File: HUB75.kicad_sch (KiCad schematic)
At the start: 12 parts, among them J2 Conn_02x08_Odd_Even, U10 SN74LVC8T245, U11 SN74LVC8T245, U2 ICE40HX8K-BG121

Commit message: Routing changes, pullups, etc
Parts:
- C30, C37, C38, J2, JP2, U10, U11, U2: Source (none) -> ANY
- R16, R17, R18, R19: value R -> 10k; Source (none) -> ANY
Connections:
- net GND: now also R16.1, R17.1
- net VCC: no longer R16.1, R17.1

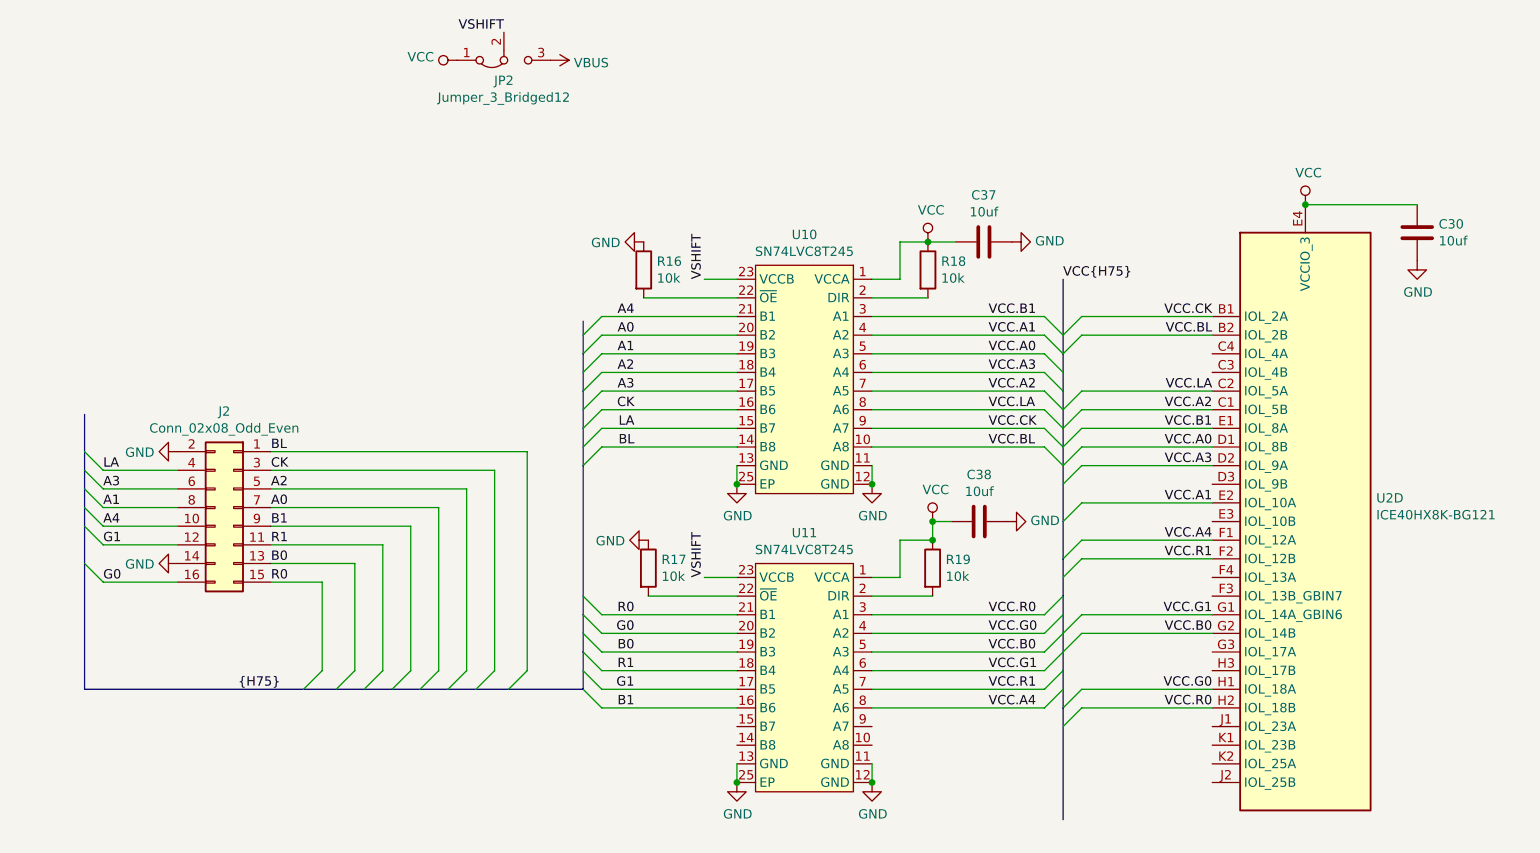
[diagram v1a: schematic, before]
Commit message: Routing cleanup, fix primary transformer
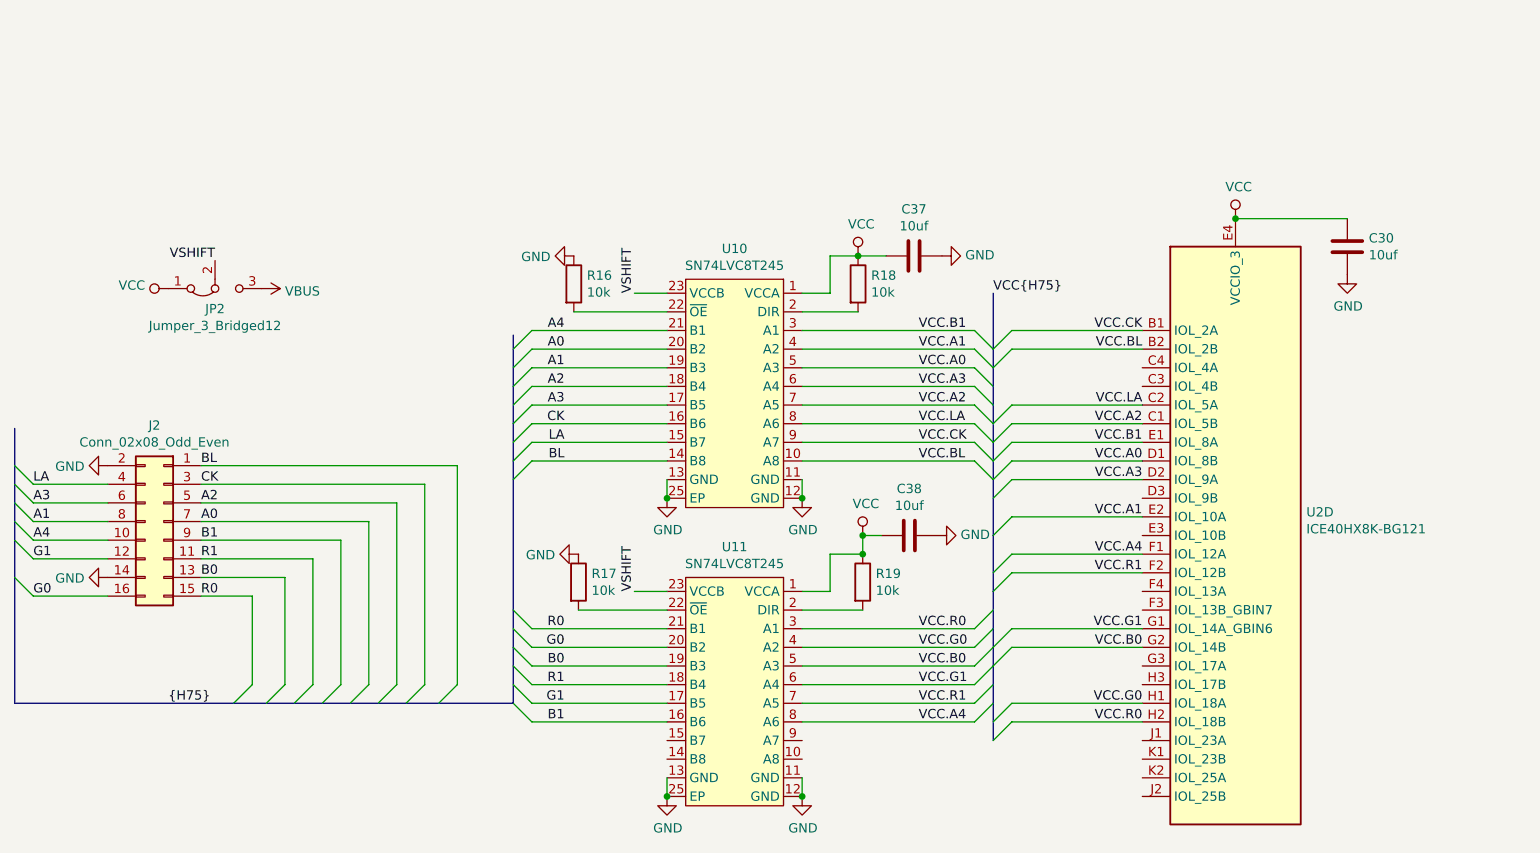
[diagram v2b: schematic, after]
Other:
- moved on the sheet: C30, C37, C38, J2, JP2, R16, R17, R18, R19, U10, U11, U2D

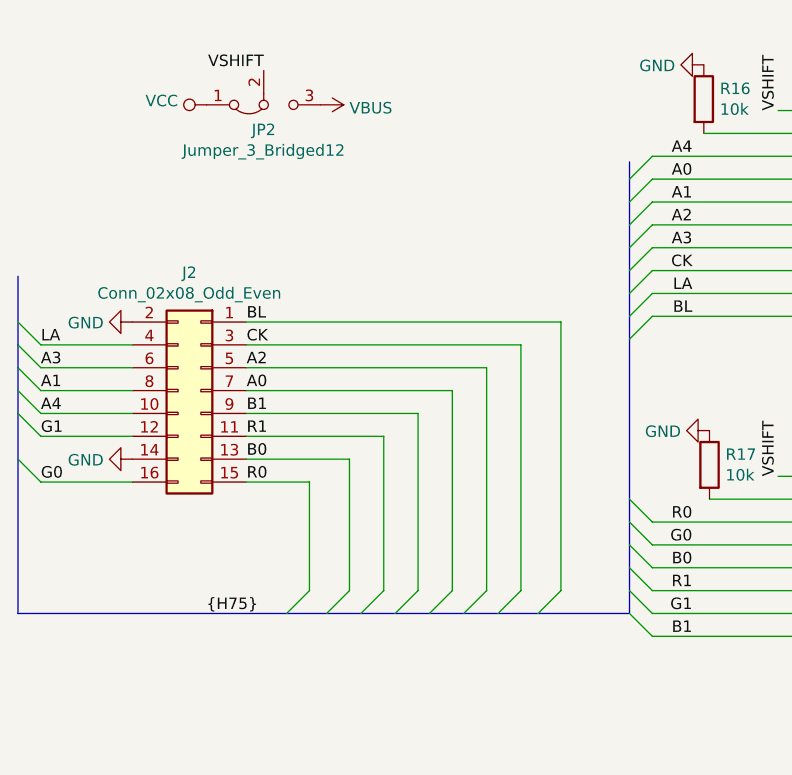
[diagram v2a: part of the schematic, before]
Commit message: Change PoE controller to NCP1081
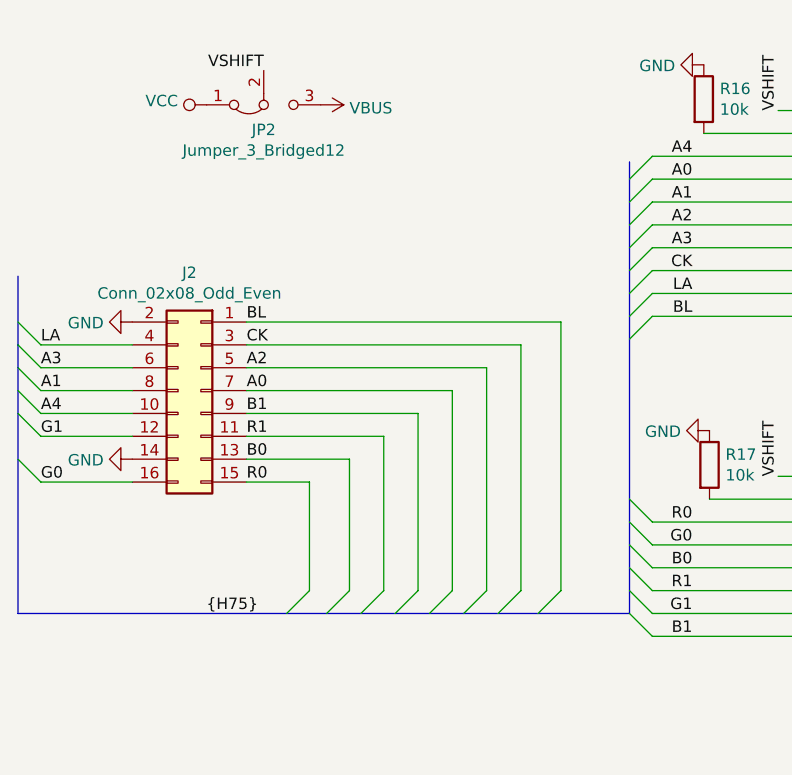
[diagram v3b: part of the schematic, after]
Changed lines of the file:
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@@
-(kicad_sch (version 20200512) (host eeschema "5.99.0-unknown-eae0c14~101~ubuntu20.04.1")
-  (page 7 7)
+(kicad_sch (version 20200608) (host eeschema "5.99.0-unknown-8bd9b26~101~ubuntu20.04.1")
+  (page 1 7)
   (paper "A4")
   (title_block
@@
     (stroke (width 0) (type solid) (color 0 0 0 0))
   )
-  (bus (pts (xy 53.34 129.54) (xy 83.185 129.54))
-    (stroke (width 0) (type solid) (color 0 0 0 0))
-  )
-  (bus (pts (xy 83.185 129.54) (xy 91.44 129.54))
-    (stroke (width 0) (type solid) (color 0 0 0 0))
-  )
-  (bus (pts (xy 91.44 129.54) (xy 99.06 129.54))
-    (stroke (width 0) (type solid) (color 0 0 0 0))
-  )
-  (bus (pts (xy 99.06 129.54) (xy 106.68 129.54))
-    (stroke (width 0) (type solid) (color 0 0 0 0))
-  )
-  (bus (pts (xy 106.68 129.54) (xy 121.285 129.54))
-    (stroke (width 0) (type solid) (color 0 0 0 0))
-  )
-  (bus (pts (xy 121.285 79.375) (xy 121.285 81.28))
-    (stroke (width 0) (type solid) (color 0 0 0 0))
-  )
-  (bus (pts (xy 121.285 81.28) (xy 121.285 86.36))
-    (stroke (width 0) (type solid) (color 0 0 0 0))
-  )
-  (bus (pts (xy 121.285 86.36) (xy 121.285 91.44))
+  (bus (pts (xy 53.34 129.54) (xy 87.63 129.54))
+    (stroke (width 0) (type solid) (color 0 0 0 0))
+  )
+  (bus (pts (xy 87.63 129.54) (xy 95.25 129.54))
+    (stroke (width 0) (type solid) (color 0 0 0 0))
+  )
+  (bus (pts (xy 95.25 129.54) (xy 102.87 129.54))
+    (stroke (width 0) (type solid) (color 0 0 0 0))
+  )
+  (bus (pts (xy 102.87 129.54) (xy 111.125 129.54))
+    (stroke (width 0) (type solid) (color 0 0 0 0))
+  )
+  (bus (pts (xy 111.125 129.54) (xy 121.285 129.54))
+    (stroke (width 0) (type solid) (color 0 0 0 0))
+  )
+  (bus (pts (xy 121.285 79.375) (xy 121.285 83.82))
+    (stroke (width 0) (type solid) (color 0 0 0 0))
+  )
+  (bus (pts (xy 121.285 83.82) (xy 121.285 88.9))
+    (stroke (width 0) (type solid) (color 0 0 0 0))
+  )
+  (bus (pts (xy 121.285 88.9) (xy 121.285 91.44))
     (stroke (width 0) (type solid) (color 0 0 0 0))
   )
@@
     (stroke (width 0) (type solid) (color 0 0 0 0))
   )
-  (bus (pts (xy 121.285 121.92) (xy 121.285 124.46))
-    (stroke (width 0) (type solid) (color 0 0 0 0))
-  )
-  (bus (pts (xy 121.285 124.46) (xy 121.285 129.54))
+  (bus (pts (xy 121.285 121.92) (xy 121.285 127))
+    (stroke (width 0) (type solid) (color 0 0 0 0))
+  )
+  (bus (pts (xy 121.285 127) (xy 121.285 129.54))
     (stroke (width 0) (type solid) (color 0 0 0 0))
   )
@@
   )
   (symbol (lib_id "power:VCC") (at 74.295 73.025 90) (unit 1)
+    (in_bom yes) (on_board yes)
     (property "Reference" "#PWR0160" (id 0) (at 78.105 73.025 0)
       (effects (font (size 1.27 1.27)) hide)
@@
   )
   (symbol (lib_id "power:VCC") (at 168.275 68.58 0) (unit 1)
+    (in_bom yes) (on_board yes)
     (property "Reference" "#PWR0158" (id 0) (at 168.275 72.39 0)
       (effects (font (size 1.27 1.27)) hide)
@@
   )
   (symbol (lib_id "power:VCC") (at 168.91 106.68 0) (unit 1)
+    (in_bom yes) (on_board yes)
     (property "Reference" "#PWR0157" (id 0) (at 168.91 110.49 0)
       (effects (font (size 1.27 1.27)) hide)
@@
   )
   (symbol (lib_id "power:VCC") (at 219.71 63.5 0) (unit 1)
+    (in_bom yes) (on_board yes)
     (property "Reference" "#PWR0137" (id 0) (at 219.71 67.31 0)
       (effects (font (size 1.27 1.27)) hide)
@@
   )
   (symbol (lib_id "power:VBUS") (at 86.995 73.025 270) (unit 1)
+    (in_bom yes) (on_board yes)
     (property "Reference" "#PWR0156" (id 0) (at 83.185 73.025 0)
       (effects (font (size 1.27 1.27)) hide)
@@
   )
   (symbol (lib_id "power:GND") (at 66.04 97.155 270) (unit 1)
+    (in_bom yes) (on_board yes)
     (property "Reference" "#PWR0133" (id 0) (at 59.69 97.155 0)
       (effects (font (size 1.27 1.27)) hide)
@@
   )
   (symbol (lib_id "power:GND") (at 66.04 112.395 270) (unit 1)
+    (in_bom yes) (on_board yes)
     (property "Reference" "#PWR0132" (id 0) (at 59.69 112.395 0)
       (effects (font (size 1.27 1.27)) hide)
@@
   )
   (symbol (lib_id "power:GND") (at 129.54 68.58 270) (unit 1)
+    (in_bom yes) (on_board yes)
     (property "Reference" "#PWR0124" (id 0) (at 123.19 68.58 0)
       (effects (font (size 1.27 1.27)) hide)
@@
   )
   (symbol (lib_id "power:GND") (at 130.175 109.22 270) (unit 1)
+    (in_bom yes) (on_board yes)
     (property "Reference" "#PWR0155" (id 0) (at 123.825 109.22 0)
       (effects (font (size 1.27 1.27)) hide)
@@
   )
   (symbol (lib_id "power:GND") (at 142.24 101.6 0) (unit 1)
+    (in_bom yes) (on_board yes)
     (property "Reference" "#PWR0153" (id 0) (at 142.24 107.95 0)
       (effects (font (size 1.27 1.27)) hide)
@@
   )
   (symbol (lib_id "power:GND") (at 142.24 142.24 0) (unit 1)
+    (in_bom yes) (on_board yes)
     (property "Reference" "#PWR0154" (id 0) (at 142.24 148.59 0)
       (effects (font (size 1.27 1.27)) hide)
@@
   )
   (symbol (lib_id "power:GND") (at 160.655 101.6 0) (unit 1)
+    (in_bom yes) (on_board yes)
     (property "Reference" "#PWR0152" (id 0) (at 160.655 107.95 0)
       (effects (font (size 1.27 1.27)) hide)
@@
   )
   (symbol (lib_id "power:GND") (at 160.655 142.24 0) (unit 1)
+    (in_bom yes) (on_board yes)
     (property "Reference" "#PWR0151" (id 0) (at 160.655 148.59 0)
       (effects (font (size 1.27 1.27)) hide)
@@
   )
   (symbol (lib_id "power:GND") (at 179.07 106.68 90) (unit 1)
+    (in_bom yes) (on_board yes)
     (property "Reference" "#PWR0180" (id 0) (at 185.42 106.68 0)
       (effects (font (size 1.27 1.27)) hide)
@@
   )
   (symbol (lib_id "power:GND") (at 179.705 68.58 90) (unit 1)
+    (in_bom yes) (on_board yes)
     (property "Reference" "#PWR0179" (id 0) (at 186.055 68.58 0)
       (effects (font (size 1.27 1.27)) hide)
@@
   )
   (symbol (lib_id "power:GND") (at 234.95 71.12 0) (unit 1)
+    (in_bom yes) (on_board yes)
     (property "Reference" "#PWR0168" (id 0) (at 234.95 77.47 0)
       (effects (font (size 1.27 1.27)) hide)
@@
   )
   (symbol (lib_id "Device:R") (at 129.54 72.39 0) (unit 1)
+    (in_bom yes) (on_board yes)
     (property "Reference" "R16" (id 0) (at 131.3181 71.2406 0)
       (effects (font (size 1.27 1.27)) (justify left))
@@
   )
   (symbol (lib_id "Device:R") (at 130.175 113.03 0) (unit 1)
+    (in_bom yes) (on_board yes)
     (property "Reference" "R17" (id 0) (at 131.9531 111.8806 0)
       (effects (font (size 1.27 1.27)) (justify left))
@@
   )
   (symbol (lib_id "Device:R") (at 168.275 72.39 0) (unit 1)
+    (in_bom yes) (on_board yes)
     (property "Reference" "R18" (id 0) (at 170.0531 71.2406 0)
       (effects (font (size 1.27 1.27)) (justify left))
@@
   )
   (symbol (lib_id "Device:R") (at 168.91 113.03 0) (unit 1)
+    (in_bom yes) (on_board yes)
     (property "Reference" "R19" (id 0) (at 170.6881 111.8806 0)
       (effects (font (size 1.27 1.27)) (justify left))
@@
   )
   (symbol (lib_id "Device:C") (at 175.26 106.68 90) (unit 1)
+    (in_bom yes) (on_board yes)
     (property "Reference" "C38" (id 0) (at 175.26 100.311 90))
     (property "Value" "10uf" (id 1) (at 175.26 102.6095 90))
@@
   )
   (symbol (lib_id "Device:C") (at 175.895 68.58 90) (unit 1)
+    (in_bom yes) (on_board yes)
     (property "Reference" "C37" (id 0) (at 175.895 62.2108 90))
     (property "Value" "10uf" (id 1) (at 175.895 64.5095 90))
@@
   )
   (symbol (lib_id "Device:C") (at 234.95 67.31 0) (unit 1)
+    (in_bom yes) (on_board yes)
     (property "Reference" "C30" (id 0) (at 237.8711 66.1606 0)
       (effects (font (size 1.27 1.27)) (justify left))
@@
   )
   (symbol (lib_id "Jumper:Jumper_3_Bridged12") (at 80.645 73.025 0) (mirror x) (unit 1)
+    (in_bom yes) (on_board yes)
     (property "Reference" "JP2" (id 0) (at 80.645 75.8 0))
     (property "Value" "Jumper_3_Bridged12" (id 1) (at 80.645 78.0987 0))
@@
   )
   (symbol (lib_id "Connector_Generic:Conn_02x08_Odd_Even") (at 73.66 104.775 0) (mirror y) (unit 1)
+    (in_bom yes) (on_board yes)
     (property "Reference" "J2" (id 0) (at 72.39 91.6748 0))
     (property "Value" "Conn_02x08_Odd_Even" (id 1) (at 72.39 93.9735 0))
@@
   )
   (symbol (lib_id "h75_poe:SN74LVC8T245") (at 151.13 71.755 0) (mirror y) (unit 1)
+    (in_bom yes) (on_board yes)
     (property "Reference" "U10" (id 0) (at 151.4475 67.5958 0))
     (property "Value" "SN74LVC8T245" (id 1) (at 151.4475 69.8945 0))
@@
   )
   (symbol (lib_id "h75_poe:SN74LVC8T245") (at 151.13 112.395 0) (mirror y) (unit 1)
+    (in_bom yes) (on_board yes)
     (property "Reference" "U11" (id 0) (at 151.4475 108.2358 0))
     (property "Value" "SN74LVC8T245" (id 1) (at 151.4475 110.5345 0))
@@
   )
   (symbol (lib_id "FPGA_Lattice:ICE40HX8K-BG121") (at 219.71 106.68 0) (unit 4)
+    (in_bom yes) (on_board yes)
     (property "Reference" "U2" (id 0) (at 229.3621 103.4986 0)
       (effects (font (size 1.27 1.27)) (justify left))

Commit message: Add missing detection resistor
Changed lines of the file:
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@@
-(kicad_sch (version 20200608) (host eeschema "5.99.0-unknown-60915fb~101~ubuntu20.04.1")
+(kicad_sch (version 20200608) (host eeschema "5.99.0-unknown-e164269~101~ubuntu20.04.1")
   (page 1 7)
   (paper "A4")
@@
     (stroke (width 0) (type solid) (color 0 0 0 0))
   )
-  (bus (pts (xy 102.87 129.54) (xy 111.125 129.54))
-    (stroke (width 0) (type solid) (color 0 0 0 0))
-  )
-  (bus (pts (xy 111.125 129.54) (xy 121.285 129.54))
-    (stroke (width 0) (type solid) (color 0 0 0 0))
-  )
+  (bus (pts (xy 102.87 129.54) (xy 106.68 129.54))
+    (stroke (width 0) (type solid) (color 0 0 0 0))
+  )
+  (bus (pts (xy 106.68 129.54) (xy 121.285 129.54))
+    (stroke (width 0) (type solid) (color 0 0 0 0))
+  )

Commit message: Fix SOT-89-3 footprint
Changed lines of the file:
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@@
-(kicad_sch (version 20200618) (host eeschema "5.99.0-unknown-b48a627~101~ubuntu20.04.1")
+(kicad_sch (version 20200618) (host eeschema "5.99.0-unknown-19b7755~101~ubuntu20.04.1")
   (page 1 7)
   (paper "A4")
@@
     (stroke (width 0) (type solid) (color 0 0 0 0))
   )
-  (bus (pts (xy 102.87 129.54) (xy 106.68 129.54))
-    (stroke (width 0) (type solid) (color 0 0 0 0))
-  )
-  (bus (pts (xy 106.68 129.54) (xy 121.285 129.54))
-    (stroke (width 0) (type solid) (color 0 0 0 0))
-  )
+  (bus (pts (xy 102.87 129.54) (xy 111.125 129.54))
+    (stroke (width 0) (type solid) (color 0 0 0 0))
+  )
+  (bus (pts (xy 111.125 129.54) (xy 121.285 129.54))
+    (stroke (width 0) (type solid) (color 0 0 0 0))
+  )

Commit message: Swap low voltage caps, remove hv side LC filter
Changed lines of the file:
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@@
-(kicad_sch (version 20200618) (host eeschema "5.99.0-unknown-19b7755~101~ubuntu20.04.1")
+(kicad_sch (version 20200618) (host eeschema "5.99.0-unknown-af8f05d~101~ubuntu20.04.1")
   (page 1 7)
   (paper "A4")
@@
     (stroke (width 0) (type solid) (color 0 0 0 0))
   )
-  (bus (pts (xy 102.87 129.54) (xy 111.125 129.54))
-    (stroke (width 0) (type solid) (color 0 0 0 0))
-  )
-  (bus (pts (xy 111.125 129.54) (xy 121.285 129.54))
-    (stroke (width 0) (type solid) (color 0 0 0 0))
-  )
+  (bus (pts (xy 102.87 129.54) (xy 106.68 129.54))
+    (stroke (width 0) (type solid) (color 0 0 0 0))
+  )
+  (bus (pts (xy 106.68 129.54) (xy 121.285 129.54))
+    (stroke (width 0) (type solid) (color 0 0 0 0))
+  )
